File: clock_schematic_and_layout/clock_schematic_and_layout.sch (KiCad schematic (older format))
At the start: 53 parts, among them M1 LED, M2 LED, M3 LED, M4 LED, M5 LED, M6 LED

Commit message: Made further adjustment to comment.
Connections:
- net at U?.14 (PD0): now also R330.1
- net at U?.15 (PD1): now also R330.1
- net at U?.16 (PD2): now also R330.1
- net at U?.17 (PD3): now also R330.1
- net at U?.18 (PD4): now also R330.1
- net at U?.19 (PD5): now also R330.1
- net at U?.22 (PC0): now also R330.1
- net at U?.33 (PA7): now also R330.1
- net at U?.34 (PA6): now also R330.1
- net at U?.35 (PA5): now also R?.1
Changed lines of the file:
@@
 Wire Wire Line
 	6350 1750 6100 1750
+Wire Wire Line
+	7650 4350 6750 4350
+Wire Wire Line
+	6750 4350 6750 7500
+Wire Wire Line
+	6750 7500 2550 7500
+Wire Wire Line
+	2550 7500 2550 1000
+Wire Wire Line
+	2550 1000 2050 1000
+Wire Wire Line
+	7650 4250 6700 4250
+Wire Wire Line
+	6700 4250 6700 7450
+Wire Wire Line
+	6700 7450 2500 7450
+Wire Wire Line
+	2500 7450 2500 1750
+Wire Wire Line
+	2500 1750 2050 1750
+Wire Wire Line
+	7650 4150 6650 4150
+Wire Wire Line
+	6650 4150 6650 7400
+Wire Wire Line
+	6650 7400 2450 7400
+Wire Wire Line
+	2450 7400 2450 2600
+Wire Wire Line
+	2450 2600 2050 2600
+Wire Wire Line
+	7650 4050 6600 4050
+Wire Wire Line
+	6600 4050 6600 7350
+Wire Wire Line
+	6600 7350 2400 7350
+Wire Wire Line
+	2400 7350 2400 3400
+Wire Wire Line
+	2400 3400 2050 3400
+Wire Wire Line
+	7650 3950 6550 3950
+Wire Wire Line
+	6550 3950 6550 7300
+Wire Wire Line
+	6550 7300 2350 7300
+Wire Wire Line
+	2350 7300 2350 4300
+Wire Wire Line
+	2350 4300 2050 4300
+Wire Wire Line
+	7650 3850 6450 3850
+Wire Wire Line
+	6450 3850 6450 7250
+Wire Wire Line
+	6450 7250 2300 7250
+Wire Wire Line
+	2300 7250 2300 5200
+Wire Wire Line
+	2300 5200 2050 5200
+Wire Wire Line
+	7650 1650 6400 1650
+Wire Wire Line
+	6400 1650 6400 6050
+Wire Wire Line
+	6400 6050 6100 6050
+Wire Wire Line
+	7650 1750 6450 1750
+Wire Wire Line
+	6450 1750 6450 650
+Wire Wire Line
+	6450 650  5150 650
+Wire Wire Line
+	5150 650  5150 5950
+Wire Wire Line
+	5150 5950 4700 5950
+Wire Wire Line
+	4700 5950 4700 6050
+Wire Wire Line
+	4700 6050 4100 6050
+Wire Wire Line
+	7650 1850 6500 1850
+Wire Wire Line
+	6500 1850 6500 600
+Wire Wire Line
+	6500 600  3250 600
+Wire Wire Line
+	3250 600  3250 5950
+Wire Wire Line
+	3250 5950 2650 5950
+Wire Wire Line
+	2650 5950 2650 6050
+Wire Wire Line
+	2650 6050 2050 6050
+Wire Wire Line
+	4150 2950 4150 5200
+Wire Wire Line
+	4150 5200 4100 5200
+Wire Wire Line
+	4150 2950 7650 2950
 $EndSCHEMATC

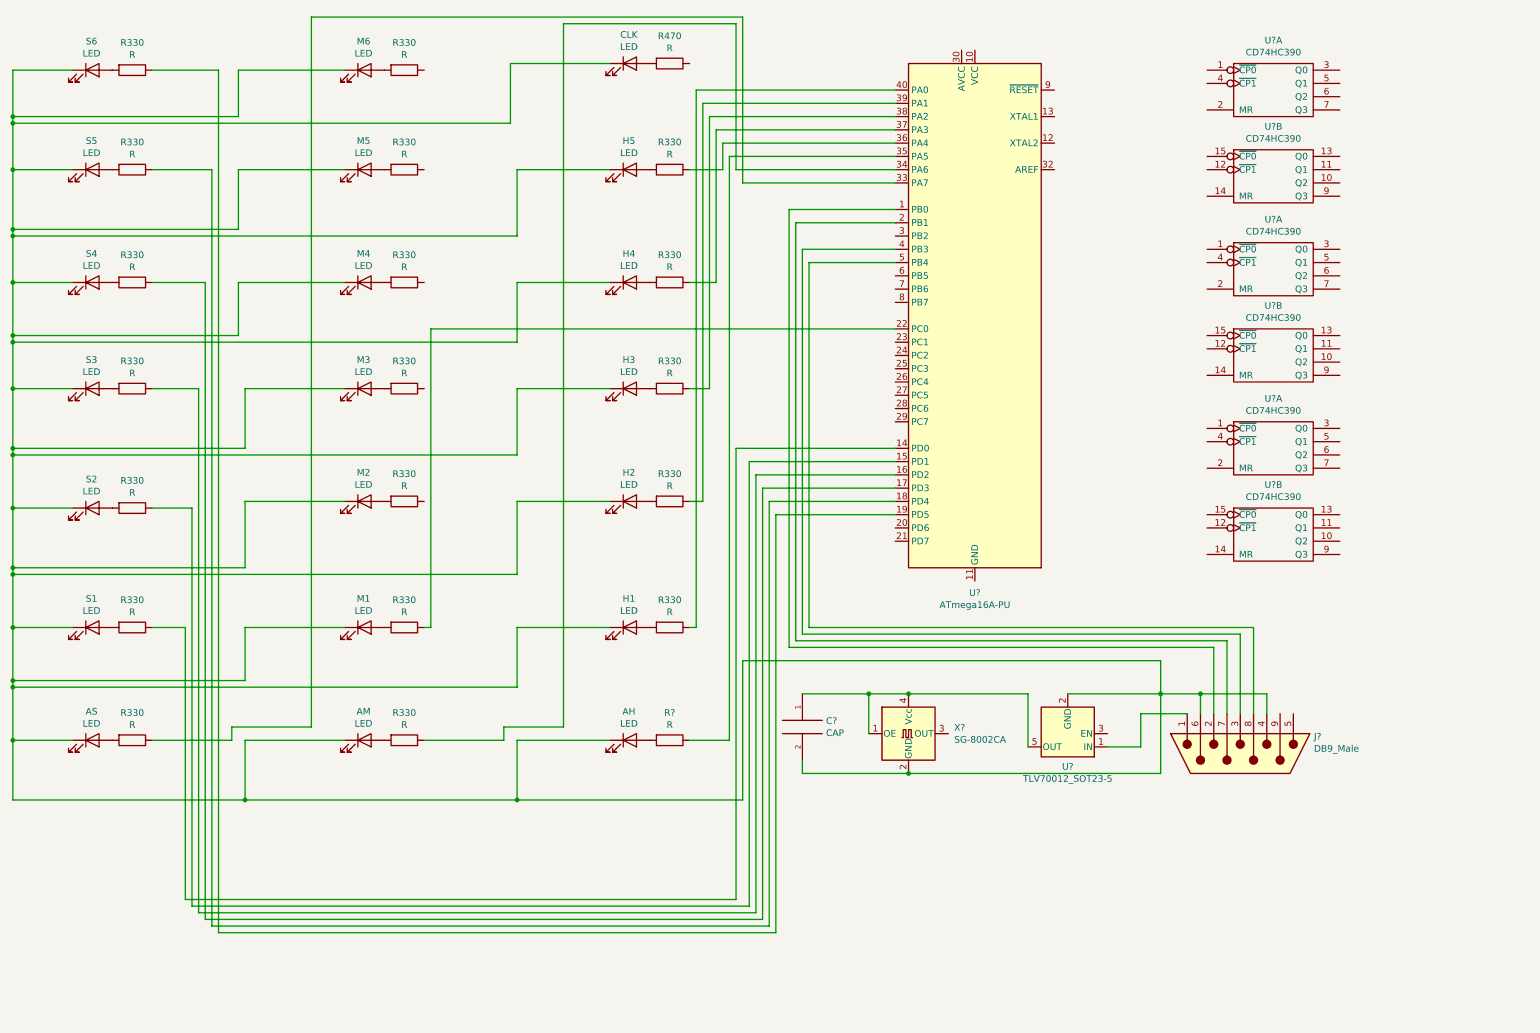
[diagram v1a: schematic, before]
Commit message: Removed erronious jump from ADJUST_TIME_DOWN_PROPER sub routine (also have done more work on schematics)
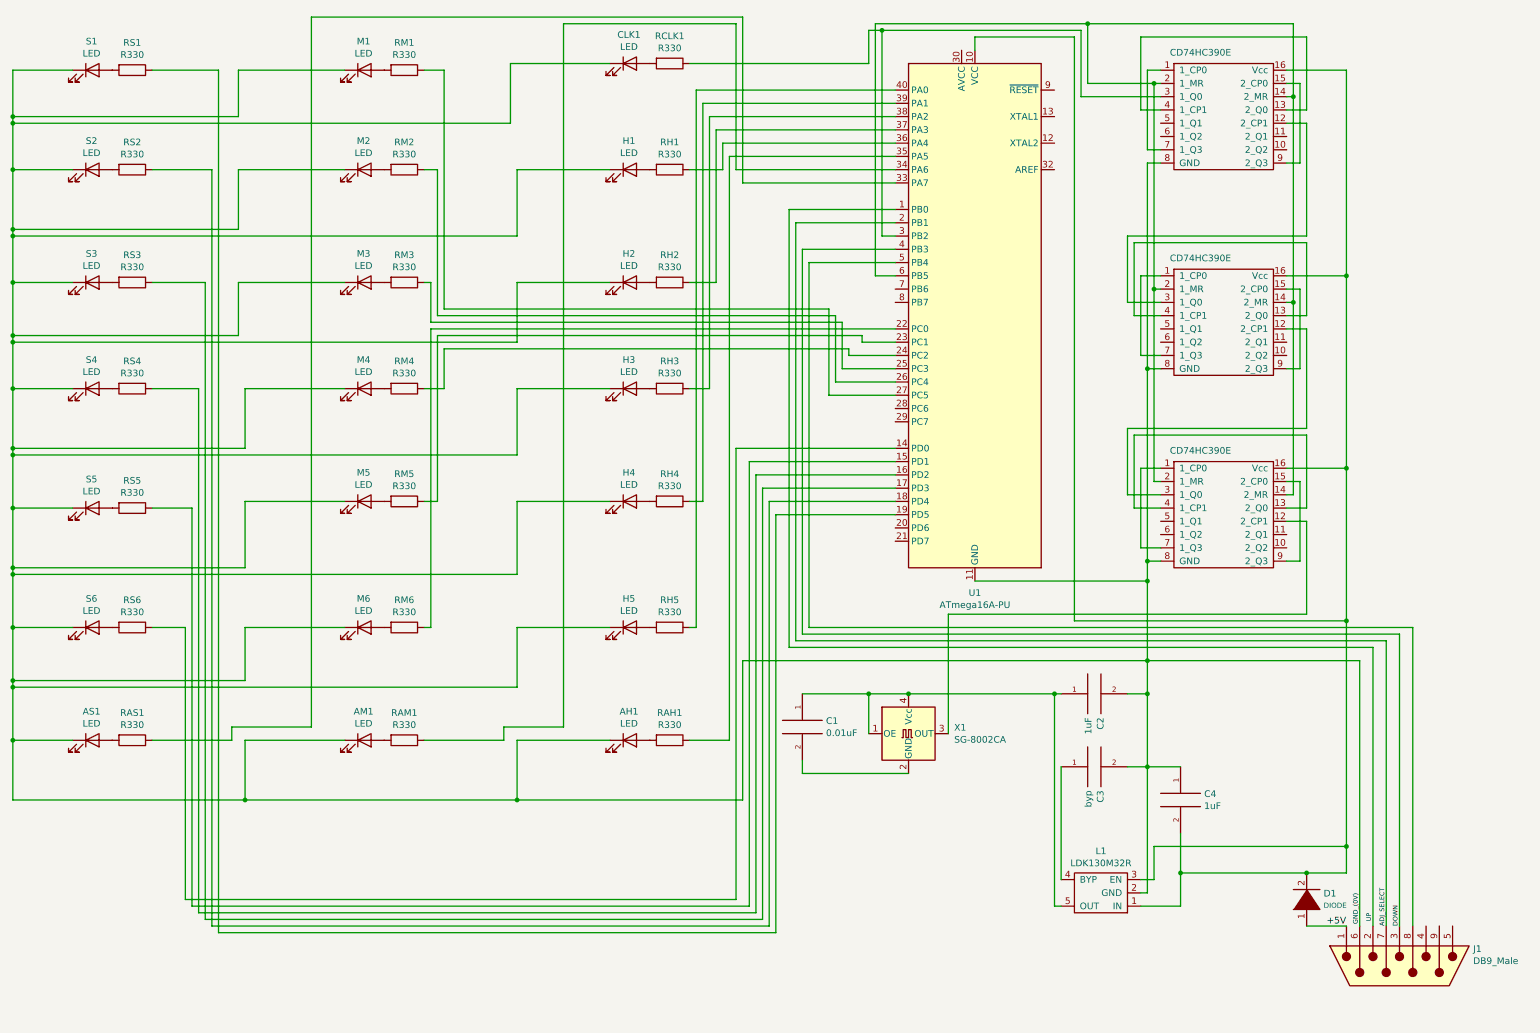
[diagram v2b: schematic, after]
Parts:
- removed U? (x6): CD74HC390, symbol CD74HCxx:CD74HC390
- removed U?: TLV70012_SOT23-5, Package_TO_SOT_SMD:SOT-23-5, symbol Regulator_Linear:TLV70012_SOT23-5
- added C2, C4: 1uF, symbol pspice:CAP
- added C3: byp, symbol pspice:CAP
- added CD74HC390E1, CD74HC390E2, CD74HC390E3: CD74HC390E, symbol CD74HCxx:CD74HC390E
- added D1: DIODE, symbol pspice:DIODE
- added L1: LDK130M32R, symbol CD74HCxx:LDK130M32R
- C1: renamed from C?; value CAP -> 0.01uF
- RAH1: renamed from R?; value R -> R330
- RAM1, RAS1, RH1, RH2, RH3, RH4, RH5, RM1, RM2, RM3, RM4, RM5, RM6, RS1, RS2, RS3, RS4, RS5, RS6: renamed from R330; value R -> R330
- RCLK1: renamed from R470; value R -> R330
- gave numbers to parts that had none: 3
- renumbered AH to AH1, AM to AM1, AS to AS1, CLK to CLK1, H5 to H1, H4 to H2, H2 to H4, H1 to H5, M6 to M1, M5 to M2, M4 to M3, M3 to M4, M2 to M5, M1 to M6, S6 to S1, S5 to S2, S4 to S3, S3 to S4, S2 to S5, S1 to S6
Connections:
- net UP: now reaches J1.2, U1.1 (PB0)
- net at U1.10 (VCC): now also C4.2, CD74HC390E1.16 (Vcc), CD74HC390E2.16 (Vcc), CD74HC390E3.16 (Vcc), D1.2 (A), L1.1 (IN), L1.3 (EN)
- net GND_(0V): now reaches U1.11 (GND), U1.31 (GND)
- net GND_(0V): now also AH1.1 (K), AM1.1 (K), AS1.1 (K), CLK1.1 (K), H1.1 (K), H2.1 (K), H3.1 (K), H4.1 (K), H5.1 (K), J1.6, M1.1 (K), M2.1 (K), M3.1 (K), M4.1 (K), M5.1 (K), M6.1 (K), S1.1 (K), S2.1 (K), S3.1 (K), S4.1 (K), S5.1 (K), S6.1 (K), C2.2, C3.2, C4.1, CD74HC390E1.8 (GND), CD74HC390E2.8 (GND), CD74HC390E3.8 (GND), L1.2 (GND)
- net ADJ_SELECT: now reaches J1.7, U1.2 (PB1)
- net at U1.23 (PC1): now also RM5.1
- net at U1.24 (PC2): now also RM4.1
- net at U1.25 (PC3): now also RM3.1
- net at U1.26 (PC4): now also RM2.1
- net at U1.27 (PC5): now also RM1.1
- net at U1.3 (PB2): now also RCLK1.1, CD74HC390E1.3 (1_Q0)
- net DOWN: now reaches J1.3, U1.4 (PB3)
- net at U1.6 (PB5): now also CD74HC390E1.14 (2_MR), CD74HC390E1.2 (1_MR), CD74HC390E2.14 (2_MR), CD74HC390E2.2 (1_MR), CD74HC390E3.14 (2_MR), CD74HC390E3.2 (1_MR)
- net at C1.1, X1.1 (OE), X1.4 (Vcc): now also C2.1, L1.5 (OUT)
- net at X1.3 (OUT): now also CD74HC390E3.12 (2_CP1)
- net +5V: now reaches J1.1
- net +5V: now also D1.1 (K)
- new net: C1.2, X1.2 (GND)
- new net: CD74HC390E1.1 (1_CP0), CD74HC390E1.7 (1_Q3)
- new net: CD74HC390E1.12 (2_CP1), CD74HC390E2.3 (1_Q0)
- new net: CD74HC390E1.13 (2_Q0), CD74HC390E1.4 (1_CP1)
- new net: CD74HC390E1.15 (2_CP0), CD74HC390E1.9 (2_Q3)
- new net: CD74HC390E3.1 (1_CP0), CD74HC390E3.7 (1_Q3)
- new net: CD74HC390E3.13 (2_Q0), CD74HC390E3.4 (1_CP1)
- new net: CD74HC390E3.15 (2_CP0), CD74HC390E3.9 (2_Q3)
- new net: CD74HC390E2.12 (2_CP1), CD74HC390E3.3 (1_Q0)
- new net: CD74HC390E2.1 (1_CP0), CD74HC390E2.7 (1_Q3)
- new net: CD74HC390E2.13 (2_Q0), CD74HC390E2.4 (1_CP1)
- new net: CD74HC390E2.15 (2_CP0), CD74HC390E2.9 (2_Q3)
- new net: C3.1, L1.4 (BYP)
- now unconnected: J1.4
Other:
- moved on the sheet: J1

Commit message: Finished schematic and PCB layout. Haven't properly double checked the schematic though :'( (can't be bothered haha.)
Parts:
- AH1, AM1, AS1, CLK1, H1, H2, H3, H4, H5, M1, M2, M3, M4, M5, M6, S1, S2, S3, S4, S5, S6: footprint (none) -> LED_THT:LED_D3.0mm_Horizontal_O1.27mm_Z2.0mm_Clear
- C1: footprint (none) -> Crystal:Crystal_SMD_TXC_9HT11-2Pin_2.0x1.2mm_HandSoldering
- C2, C3, C4: footprint (none) -> Capacitor_THT:CP_Radial_D4.0mm_P2.00mm
- CD74HC390E1, CD74HC390E2, CD74HC390E3: footprint (none) -> Package_DIP:DIP-16_W7.62mm_LongPads; symbol CD74HCxx:CD74HC390E -> clock_schematic_and_layout-rescue:CD74HC390E-CD74HCxx
- D1: footprint (none) -> Diode_SMD:D_MELF-RM10_Universal_Handsoldering
- J1: footprint (none) -> Connector_Dsub:DSUB-9_Female_Horizontal_P2.77x2.84mm_EdgePinOffset7.70mm_Housed_MountingHolesOffset9.12mm
- L1: footprint (none) -> Package_TO_SOT_SMD:TSOT-23-5_HandSoldering; symbol CD74HCxx:LDK130M32R -> clock_schematic_and_layout-rescue:LDK130M32R-CD74HCxx
- RAH1, RAM1, RAS1, RCLK1, RH1, RH2, RH3, RH4, RH5, RM1, RM2, RM3, RM4, RM5, RM6, RS1, RS2, RS3, RS4, RS5, RS6: footprint (none) -> Resistor_THT:R_Axial_DIN0207_L6.3mm_D2.5mm_P7.62mm_Horizontal
- X1: footprint Oscillator:Oscillator_SMD_SeikoEpson_SG8002CA-4Pin_7.0x5.0mm -> Oscillator:Oscillator_SMD_SeikoEpson_SG8002CA-4Pin_7.0x5.0mm_HandSoldering
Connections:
- net at CD74HC390E1.3 (1_Q0), U1.3 (PB2): now also J1.4; no longer RCLK1.1
- net at J1.9: now also RCLK1.1
